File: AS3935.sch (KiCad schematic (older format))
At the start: 16 parts, among them IC1 AS3935-BQFT, J1 Power, J2 A1, J3 A0, J4 Conn_01x02_Male, J5 Conn_01x03_Male, J6 Conn_01x02_Male, J7 Conn_01x05_Male

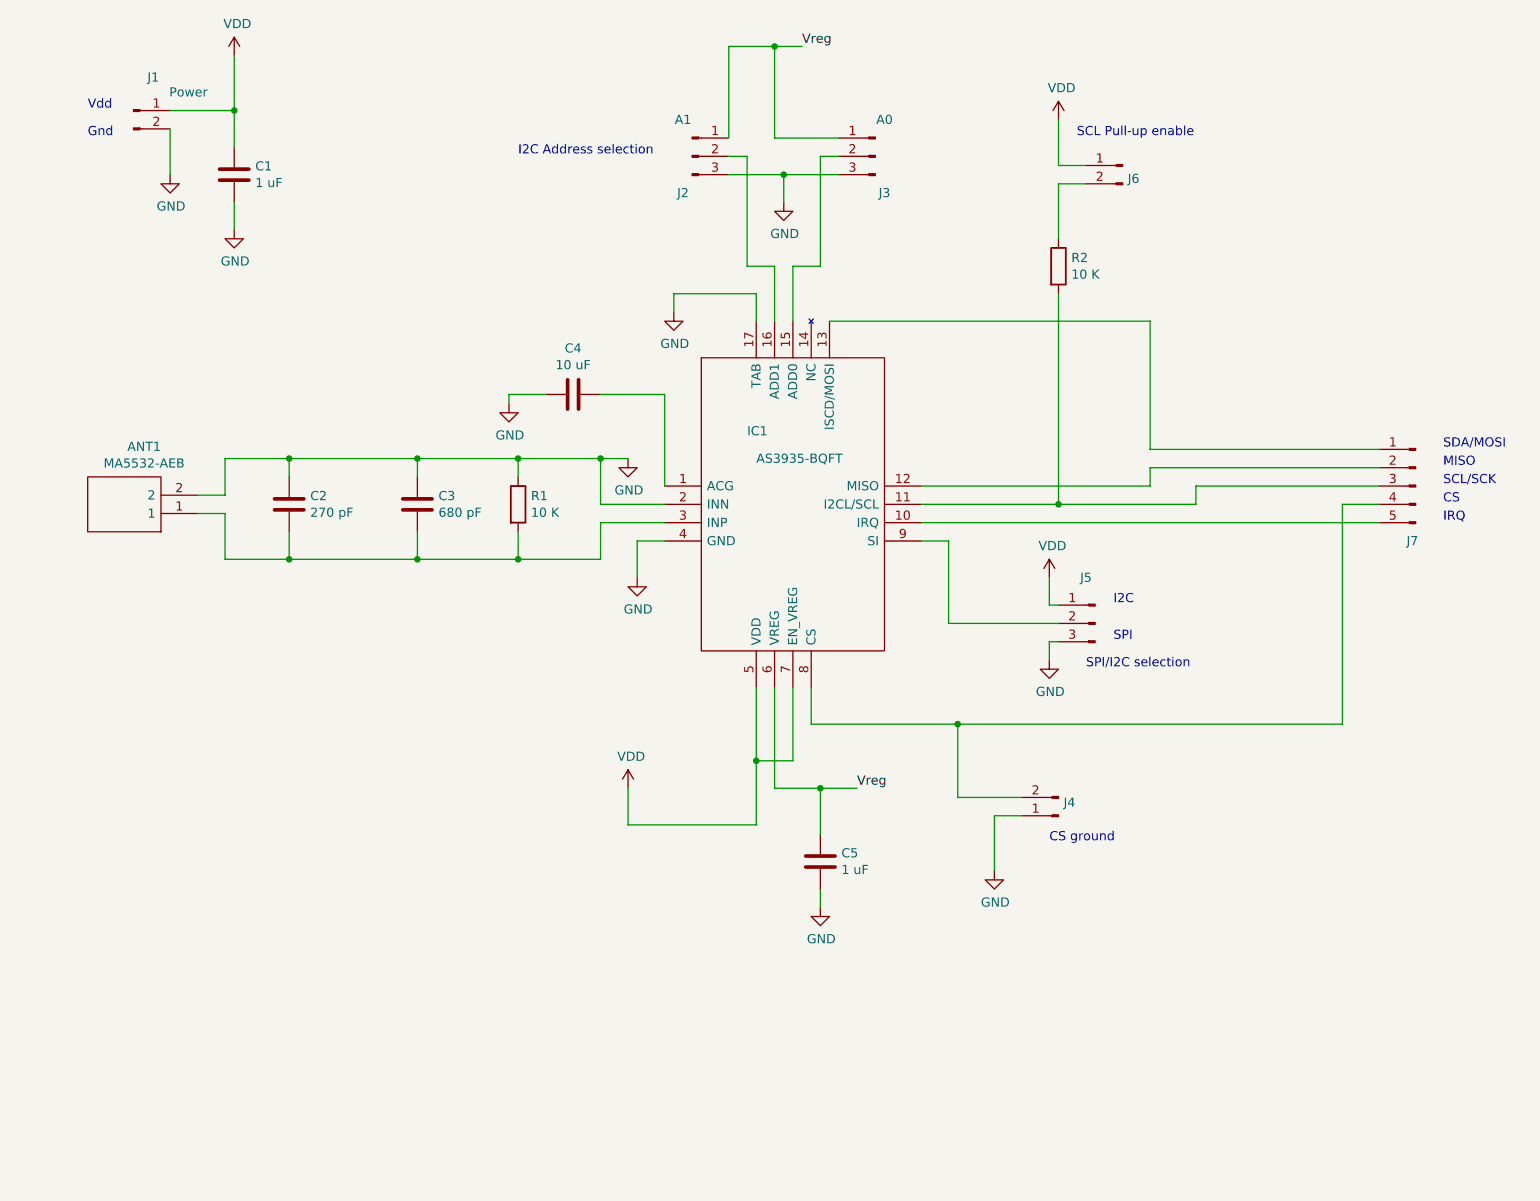
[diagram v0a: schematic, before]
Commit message: Added IRQ LED
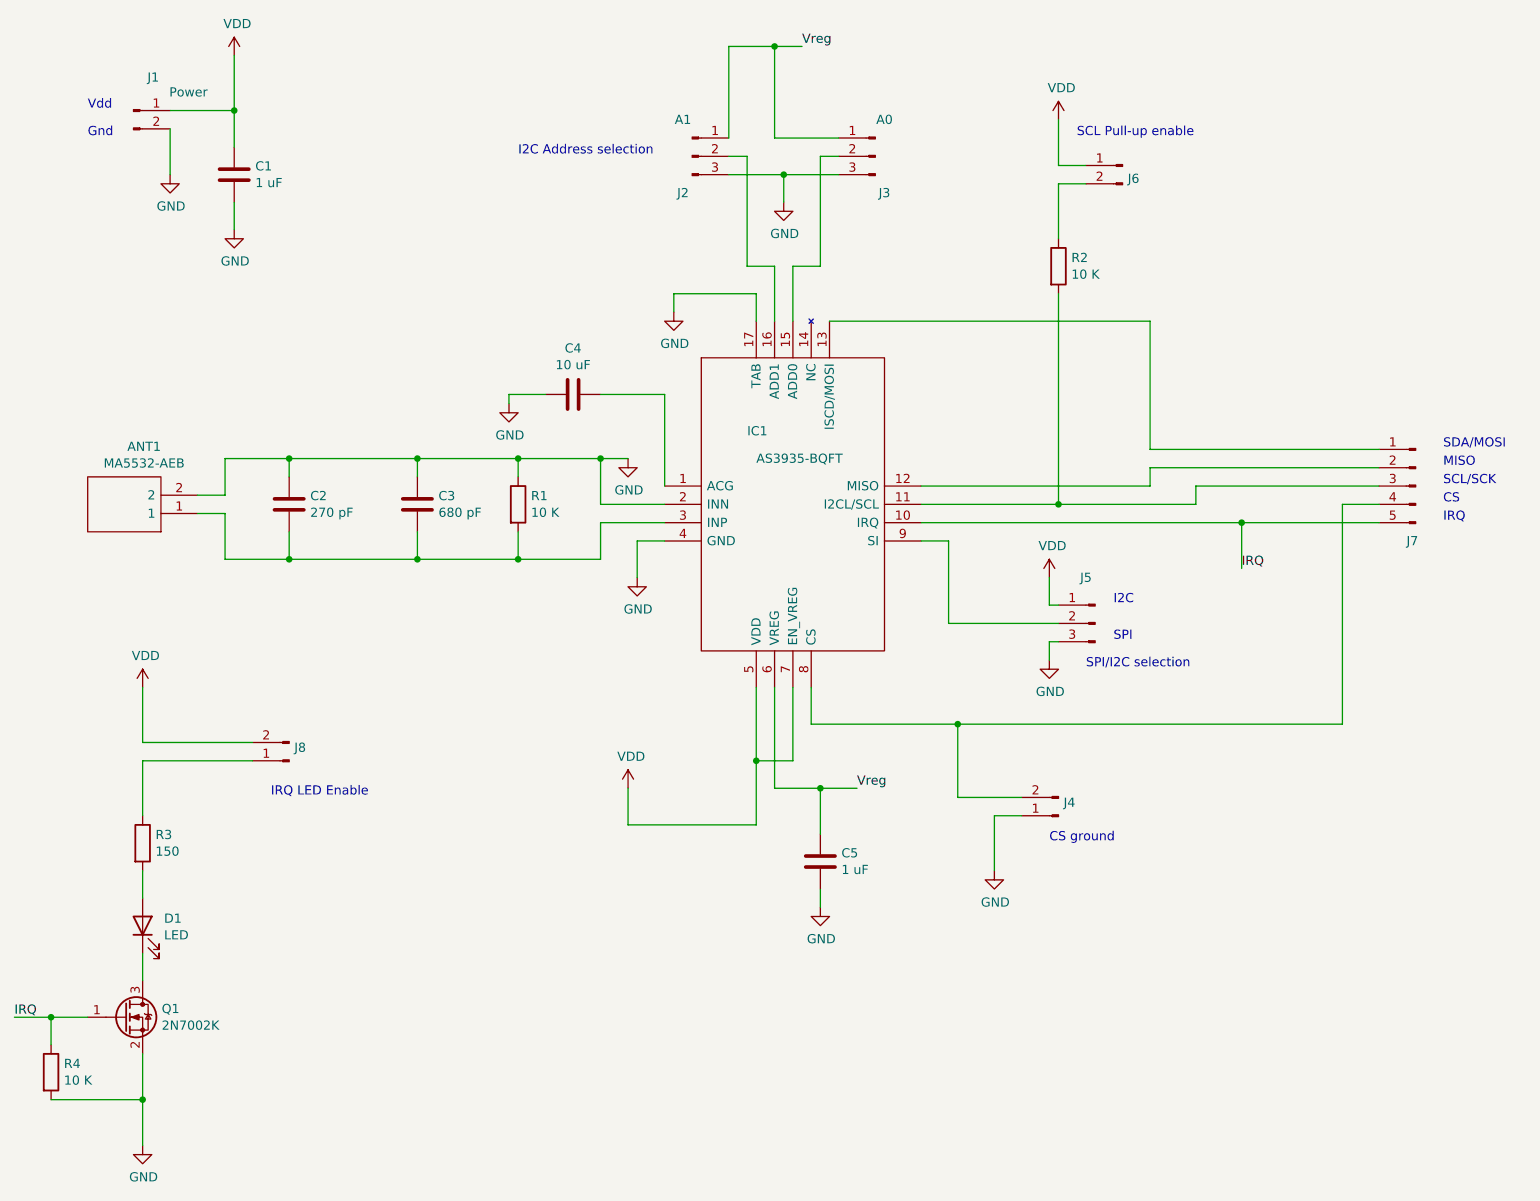
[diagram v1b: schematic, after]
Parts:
- added D1: LED, LED_SMD:LED_0805_2012Metric_Castellated, symbol Device:LED
- added J8: Conn_01x02_Male, Connector_PinHeader_2.54mm:PinHeader_1x02_P2.54mm_Vertical, symbol Connector:Conn_01x02_Male
- added Q1: 2N7002K, Package_TO_SOT_SMD:SOT-23, symbol Transistor_FET:2N7002K
- added R3: 150, Resistor_SMD:R_0603_1608Metric, symbol Device:R
- added R4: 10 K, Resistor_SMD:R_0603_1608Metric, symbol Device:R
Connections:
- net GND: now also Q1.2 (S), R4.2
- net VDD: now also J8.2 (Pin_2)
- net IRQ: now reaches IC1.10 (IRQ), J7.5 (Pin_5)
- net IRQ: now also Q1.1 (G), R4.1
- new net: J8.1 (Pin_1), R3.1
- new net: D1.2 (A), R3.2
- new net: D1.1 (K), Q1.3 (D)
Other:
- note added: "IRQ LED Enable"
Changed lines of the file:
@@
 	7900 3700 8900 3700
-Wire Wire Line
-	8900 3900 6400 3900
 Wire Wire Line
 	8700 3800 8900 3800
@@
 Text Notes 7450 4350 0    50   ~ 0
 I2C
+$Comp
+L Device:R R3
+U 1 1 5E6D3B53
+P 2150 5650
+F 0 "R3" H 2220 5696 50  0000 L CNN
+F 1 "150" H 2220 5605 50  0000 L CNN
+F 2 "Resistor_SMD:R_0603_1608Metric" V 2080 5650 50  0001 C CNN
+F 3 "~" H 2150 5650 50  0001 C CNN
+	1    2150 5650
+	1    0    0    -1
+$EndComp
+$Comp
+L Device:LED D1
+U 1 1 5E6D43DD
+P 2150 6100
+F 0 "D1" V 2189 5983 50  0000 R CNN
+F 1 "LED" V 2098 5983 50  0000 R CNN
+F 2 "LED_SMD:LED_0805_2012Metric_Castellated" H 2150 6100 50  0001 C CNN
+F 3 "~" H 2150 6100 50  0001 C CNN
+	1    2150 6100
+	0    -1   -1   0
+$EndComp
+$Comp
+L power:GND #PWR016
+U 1 1 5E6D56A6
+P 2150 7300
+F 0 "#PWR016" H 2150 7050 50  0001 C CNN
+F 1 "GND" H 2155 7127 50  0000 C CNN
+F 2 "" H 2150 7300 50  0001 C CNN
+F 3 "" H 2150 7300 50  0001 C CNN
+	1    2150 7300
+	1    0    0    -1
+$EndComp
+$Comp
+L Transistor_FET:2N7002K Q1
+U 1 1 5E6DCAE1
+P 2050 6600
+F 0 "Q1" H 2254 6646 50  0000 L CNN
+F 1 "2N7002K" H 2254 6555 50  0000 L CNN
+F 2 "Package_TO_SOT_SMD:SOT-23" H 2250 6525 50  0001 L CIN
+F 3 "https://www.diodes.com/assets/Datasheets/ds30896.pdf" H 2050 6600 50  0001 L CNN
+	1    2050 6600
+	1    0    0    -1
+$EndComp
+Wire Wire Line
+	6400 3900 8150 3900
+$Comp
+L Connector:Conn_01x02_Male J8
+U 1 1 5E7111FF
+P 2950 5200
+F 0 "J8" H 2922 5128 50  0000 R CNN
+F 1 "Conn_01x02_Male" H 3058 5290 50  0001 C CNN
+F 2 "Connector_PinHeader_2.54mm:PinHeader_1x02_P2.54mm_Vertical" H 2950 5200 50  0001 C CNN
+F 3 "~" H 2950 5200 50  0001 C CNN
+	1    2950 5200
+	-1   0    0    1
+$EndComp
+Wire Wire Line
+	2150 5500 2150 5200
+Wire Wire Line
+	2150 5200 2750 5200
+Wire Wire Line
+	2150 5950 2150 5800
+Wire Wire Line
+	2150 6400 2150 6250
+$Comp
+L power:VDD #PWR015
+U 1 1 5E726D49
+P 2150 4800
+F 0 "#PWR015" H 2150 4650 50  0001 C CNN
+F 1 "VDD" H 2167 4973 50  0000 C CNN
+F 2 "" H 2150 4800 50  0001 C CNN
+F 3 "" H 2150 4800 50  0001 C CNN
+	1    2150 4800
+	1    0    0    -1
+$EndComp
+Wire Wire Line
+	2750 5100 2150 5100
+Wire Wire Line
+	2150 5100 2150 4800
+Text Label 1450 6600 0    50   ~ 0
+IRQ
+Wire Wire Line
+	1850 6600 1650 6600
+Text Label 8150 4150 0    50   ~ 0
+IRQ
+Wire Wire Line
+	8150 4150 8150 3900
+Connection ~ 8150 3900
+Wire Wire Line
+	8150 3900 8900 3900
+Text Notes 2850 5400 0    50   ~ 0
+IRQ LED Enable
+$Comp
+L Device:R R4
+U 1 1 5E731451
+P 1650 6900
+F 0 "R4" H 1720 6946 50  0000 L CNN
+F 1 "10 K" H 1720 6855 50  0000 L CNN
+F 2 "Resistor_SMD:R_0603_1608Metric" V 1580 6900 50  0001 C CNN
+F 3 "~" H 1650 6900 50  0001 C CNN
+	1    1650 6900
+	1    0    0    -1
+$EndComp
+Wire Wire Line
+	2150 6800 2150 7050
+Wire Wire Line
+	1650 7050 2150 7050
+Connection ~ 2150 7050
+Wire Wire Line
+	2150 7050 2150 7300
+Wire Wire Line
+	1650 6750 1650 6600
+Connection ~ 1650 6600
+Wire Wire Line
+	1650 6600 1450 6600
 $EndSCHEMATC

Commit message: Adjusted pcb properties
Regenerated gerbers
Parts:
- ANT1: symbol SamacSys_Parts:MA5532-AEB -> AS3935-rescue:MA5532-AEB-SamacSys_Parts
- IC1: symbol SamacSys_Parts:AS3935-BQFT -> AS3935-rescue:AS3935-BQFT-SamacSys_Parts
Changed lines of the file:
@@
 $EndDescr
 $Comp
-L SamacSys_Parts:MA5532-AEB ANT1
+L AS3935-rescue:MA5532-AEB-SamacSys_Parts ANT1
 U 1 1 5E6A8392
 P 2450 3850
@@
 $EndComp
 $Comp
-L SamacSys_Parts:AS3935-BQFT IC1
+L AS3935-rescue:AS3935-BQFT-SamacSys_Parts IC1
 U 1 1 5E6A9DD2
 P 5000 3700

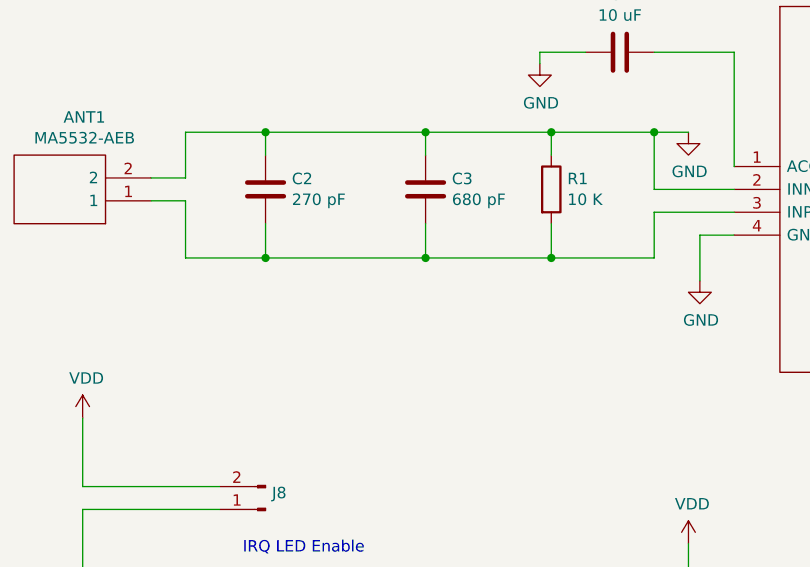
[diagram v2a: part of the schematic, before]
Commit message: Added C2 comment
The first populated board worked better with 330 pF for C2
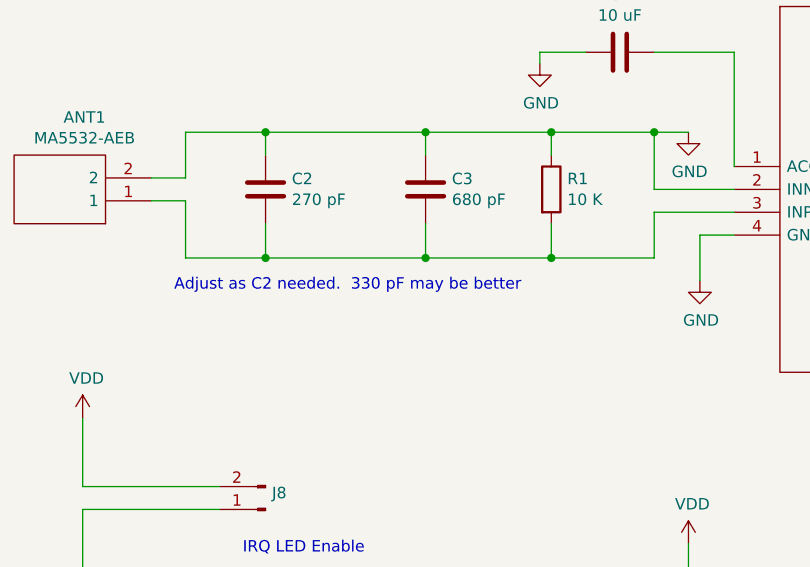
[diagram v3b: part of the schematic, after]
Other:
- note added: "Adjust as C2 needed. 330 pF may be better"
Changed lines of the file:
@@
 Wire Wire Line
 	1650 6600 1450 6600
+Text Notes 2550 4250 0    50   ~ 0
+Adjust as C2 needed.  330 pF may be better
 $EndSCHEMATC
